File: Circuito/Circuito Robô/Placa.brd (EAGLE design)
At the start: 100 x 80 mm, 7 parts, among them M1 MOTOR10MM, M2 MOTOR10MM, U1 328P, Y1 16MHz

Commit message: Conectores e Trimpots
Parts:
- added C1: 0.1uF, rcl:C075-052X106
- added C2: 1uF, resistor:085CS_1AR
- added C3: 10uF, resistor:085CS_1AR
- added D1, D2: 1N4002, diode:DO41-10
- added G1: AB9V, battery:AB9V
- added IC1: LM317MBSTT3, v-reg:SOT223
- added R2: 240Ω, resistor:M0805
- added R3: 720Ω, resistor:M0805
- added R4, R5: (no value), pot:3223W
- added X1, X2, X3, X4, X5, X6, X7: 87438-03, con-molex:87438-03
- moved M1 92.9 mm to (-35.6, 8.89)
- moved Y1 73.3 mm to (-21.6, 71.1)
- moved U1 67.4 mm to (-33.0, 45.7)
- moved M2 58.9 mm to (-49.5, 8.89)
- moved S1 56.4 mm to (-49.5, 54.6)
- moved U$1 54.7 mm to (-21.6, 8.89)
- moved R1 51.1 mm to (-29.2, 69.8)
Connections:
- removed net N$12 (its old number): M2.+, U$1.4
- removed net VCC: R1.2, U$1.12, U$1.6, U1.20, U1.21, U1.7
- new net N$13: C3.+, D2.A, IC1.1, R2.1, R3.2
- new net N$14: U1.23, X1.1
- new net N$15: U1.24, X2.1
- new net N$16: U1.25, X3.1
- new net N$17: U1.11, X5.1
- new net N$18: U1.13, X7.1
- new net N$19: U1.12, X6.1
- new net N$20: U1.6, X4.1
- new net N$21: R4.1, U$1.16
- new net N$23: M1.+, R4.2
- new net N$24: M2.+, R5.2
- new net VIN: C1.1, D1.C, G1.+, IC1.3, U$1.6
- new net VO: C2.+, D1.A, D2.C, IC1.4, R1.2, R2.2, U$1.12, U1.20, U1.21, U1.7, X1.3, X2.3, X3.3, X4.3, X5.3, X6.3, X7.3
- net GND: now also C1.2, C2.-, C3.-, G1.-, R3.1, X1.2, X2.2, X3.2, X4.2, X5.2, X6.2, X7.2; no longer U$1.19
- net N$10: now also M1.-, U$1.19; no longer M1.+
- net N$11: now also R5.1, U$1.4; no longer M1.-, U$1.16
- net N$4: now also U1.14; no longer U1.23
- net N$5: now also U1.17; no longer U1.24
- net N$6: now also U1.18; no longer U1.25
- net N$7: now also U1.19; no longer U1.26
- net N$8: now also U1.15; no longer U1.18
- net N$9: now also U1.16; no longer U1.19
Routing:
- net VO: track 0.00 -> 238.6 mm, vias 0 -> 2
- net GND: track 0.00 -> 212.1 mm
- net VIN: track 0.00 -> 91.3 mm, vias 0 -> 1
- net N$13: track 0.00 -> 84.5 mm, vias 0 -> 1
- net N$11: track 0.00 -> 84.0 mm, vias 0 -> 2
- net N$21: track 0.00 -> 70.8 mm, vias 0 -> 2
- net N$24: track 0.00 -> 67.8 mm
- net N$23: track 0.00 -> 64.5 mm, vias 0 -> 1
- net N$7: track 0.00 -> 64.0 mm, vias 0 -> 1
- net N$5: track 0.00 -> 58.5 mm, vias 0 -> 1
- net N$8: track 0.00 -> 57.8 mm, vias 0 -> 1
- net N$17: track 0.00 -> 55.4 mm, vias 0 -> 1
- net N$3: track 0.00 -> 52.5 mm
- net N$9: track 0.00 -> 51.3 mm
- net N$6: track 0.00 -> 50.1 mm, vias 0 -> 1
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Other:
- board size 100 x 80 mm -> 160 x 100 mm

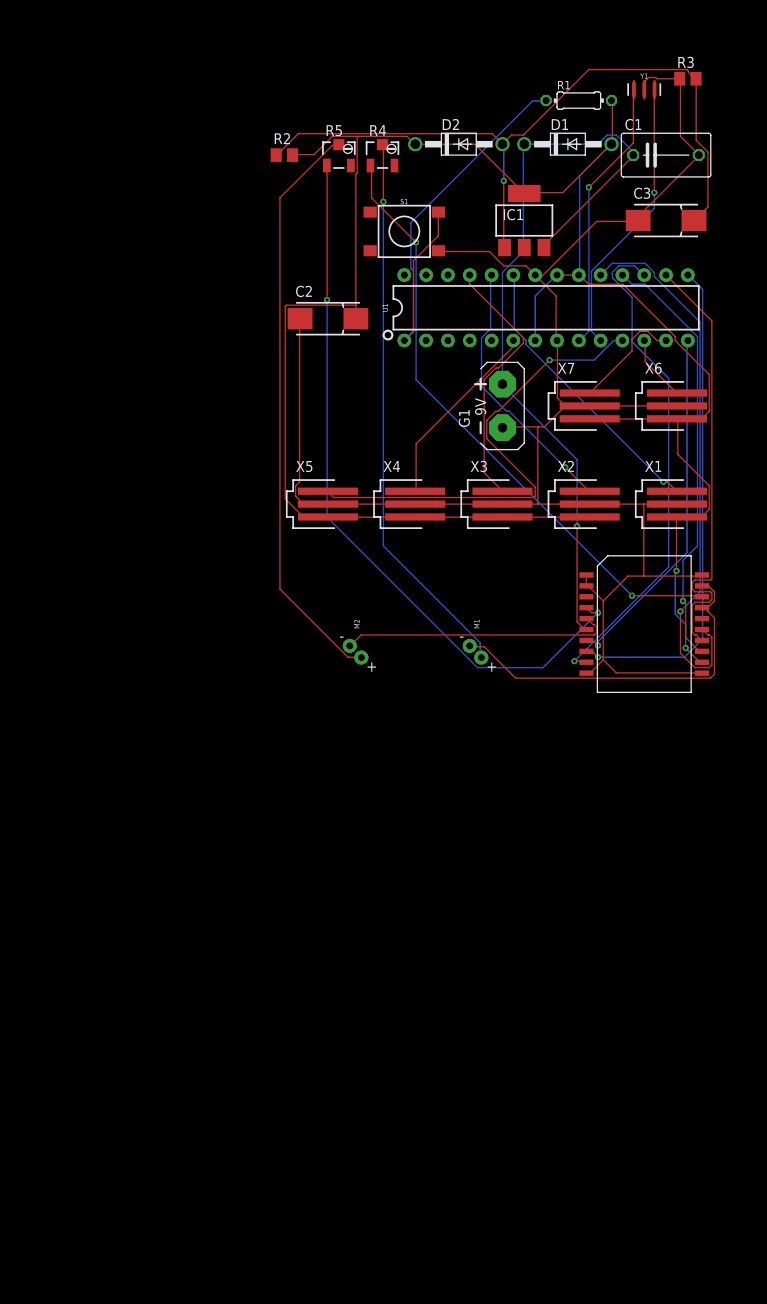
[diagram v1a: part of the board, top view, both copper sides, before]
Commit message: Adiciona TB6612 e Trimpots
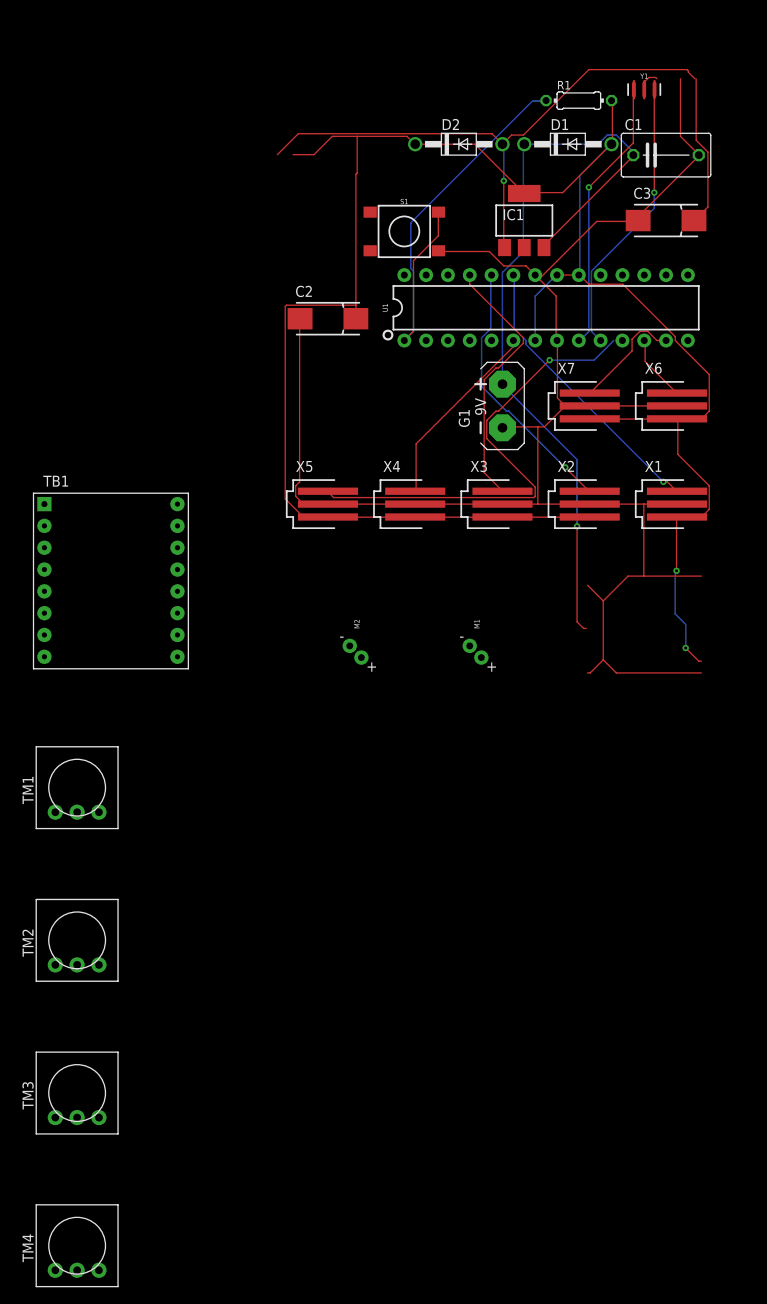
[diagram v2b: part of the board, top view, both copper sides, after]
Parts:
- removed R2: 240Ω, resistor:M0805
- removed R3: 720Ω, resistor:M0805
- removed R4, R5: (no value), pot:3223W
- removed U$1: L298P013, SparkFun-IC-Special-Function:POWERSO20
- added TB1: TB6612FNG, TB6612FNG:TB6612FNG
- added TM1, TM2, TM3, TM4: (no value), adafruit:TRIM-3386
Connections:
- removed net N$24: M2.+, R5.2
- new net N$22: TB1.PWMB, U1.11
- new net N$25: TM1.2, U1.26
- net GND: now also TB1.GND1, TM1.3, TM2.3, TM4.1; no longer R3.1, U$1.1, U$1.10, U$1.11, U$1.2, U$1.20
- net N$10: now also TB1.PWMA, U1.5; no longer M1.-, U$1.17, U$1.19
- net N$11: now also TB1.STBY, U1.16; no longer R5.1, U$1.4
- net N$12: now also TB1.BIN1, U1.17; no longer M2.-, U$1.5
- net N$13: now also TM3.1, TM4.2; no longer R2.1, R3.2
- net N$17: now also U1.4; no longer U1.11
- net N$21: now also TB1.BIN2, U1.18; no longer R4.1, U$1.16
- net N$23: now also TM2.2, U1.27; no longer M1.+, R4.2
- net N$4: now also TB1.AIN2; no longer U$1.7
- net N$5: now also TB1.AIN1, U1.15; no longer U$1.9, U1.17
- net N$6: now also M1.+, TB1.A1; no longer U$1.13, U1.18
- net N$7: now also M1.-, TB1.A2; no longer U$1.15, U1.19
- net N$8: now also M2.-, TB1.B2; no longer U$1.8, U1.15
- net N$9: now also M2.+, TB1.B1; no longer U$1.14, U1.16
- net VIN: now also TB1.VM; no longer U$1.6
- net VO: now also TB1.VCC, TM1.1, TM2.1, TM3.2; no longer R2.2, U$1.12
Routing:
- net N$11: track 84.0 -> 0.00 mm, vias 2 -> 0
- net N$21: track 70.8 -> 0.00 mm, vias 2 -> 0
- net N$24: track 67.8 -> 0.00 mm
- net N$23: track 64.5 -> 0.00 mm, vias 1 -> 0
- net N$7: track 64.0 -> 0.00 mm, vias 1 -> 0
- net N$5: track 58.5 -> 0.00 mm, vias 1 -> 0
- net N$8: track 57.8 -> 0.00 mm, vias 1 -> 0
- net N$9: track 51.3 -> 0.00 mm
- net N$6: track 50.1 -> 0.00 mm, vias 1 -> 0
- net N$10: track 43.6 -> 0.00 mm
- net N$4: track 41.5 -> 0.00 mm, vias 1 -> 0
- net N$12: track 31.6 -> 0.00 mm
- net GND: track 212.1 -> 207.5 mm
- net N$17: track 55.4 -> 54.3 mm

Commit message: PCB com 125mm
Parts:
- moved C2 206.2 mm to (143.5, 86.4)
- moved TB1 195.3 mm to (105.4, 64.8), turned to 270 degrees
- moved G1 183.4 mm to (144.8, 48.3)
- moved D2 179.1 mm to (135.9, 64.8), turned to 270 degrees
- moved D1 175.3 mm to (144.8, 64.8), turned to 90 degrees
- moved M1 170.0 mm to (113.0, 91.4)
- moved TM4 168.0 mm to (53.3, 27.9)
- moved M2 161.4 mm to (92.7, 85.1), turned to 180 degrees
- moved C1 156.0 mm to (134.6, 36.8)
- moved IC1 153.0 mm to (115.6, 31.8)
- moved TM1 151.9 mm to (35.6, 78.7)
- moved TM2 147.2 mm to (34.3, 54.6)
- moved C3 146.1 mm to (127.0, 55.9)
- moved TM3 144.5 mm to (34.3, 31.8)
- moved X5 124.5 mm to (64.8, 40.6), turned to 270 degrees
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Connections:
- net N$19: now also U1.11; no longer U1.12
- net N$22: now also U1.12; no longer U1.11
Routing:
- net VO: track 238.3 -> 454.0 mm, vias 2 -> 0
- net GND: track 207.5 -> 0.00 mm
- net N$18: track 13.1 -> 93.6 mm
- net N$25: track 0.00 -> 53.4 mm
- net N$13: track 84.2 -> 129.6 mm, vias 1 -> 0
- net N$10: track 0.00 -> 44.2 mm
- net N$23: track 0.00 -> 43.5 mm
- net N$17: track 54.3 -> 19.1 mm, vias 1 -> 0
- net N$3: track 52.5 -> 20.2 mm
- net N$2: track 31.7 -> 5.11 mm, vias 1 -> 0
- net N$1: track 31.0 -> 5.11 mm, vias 1 -> 0
- net N$7: track 0.00 -> 18.6 mm
- net N$20: track 22.4 -> 39.6 mm
- net N$9: track 0.00 -> 17.1 mm
- net N$6: track 0.00 -> 16.8 mm
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- added copper zone on layer 1, net GND
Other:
- board size 160 x 100 mm -> 125.7 x 70.8 mm
